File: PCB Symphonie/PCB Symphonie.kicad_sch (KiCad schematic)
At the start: 55 parts, among them J1 Neopixel Clavier, J2 Neopixel Indicateur batterie, SW0 SW_Push, SW1 SW_Push, SW10 SW_Push, SW11 SW_Push, SW12 SW_Push, SW13 SW_Push, SW14 SW_Push, SW15 SW_Push, SW16 SW_Push, SW17 SW_Push, SW18 SW_Push, SW19 SW_Push, SW2 SW_Push, SW20 SW_Push, SW21 SW_Push, SW22 SW_Push, SW23 SW_Push, SW24 SW_Push, SW3 SW_Push, SW4 SW_Push, SW5 SW_Push, SW6 SW_Push, SW7 SW_Push, SW8 SW_Push, SW9 SW_Push

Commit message: MAJ pcb
ajout alim remplacement esp32 par connecteur
Verifier taille condensateur (polarisation),
demander a augustin res de puissances,
replacer bouttons par piste et bornier
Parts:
- removed A1: Arduino_Nano_ESP32, Module:Arduino_Nano, symbol MCU_Module:Arduino_Nano_ESP32
- added BT1: Battery_Cell, symbol Device:Battery_Cell
- added C1, C10, C11, C12, C2, C3, C4, C5, C6, C7, C8, C9: C, symbol Device:C
- added D25, D27: LED, symbol Device:LED
- added D28: 1N4148, Diode_THT:D_DO-35_SOD27_P7.62mm_Horizontal, symbol Diode:1N4148
- added F1: Fuse, symbol Device:Fuse
- added J3: Bornier Alim Ampli, Connector:JWT_A3963_1x02_P3.96mm_Vertical, symbol Connector:Conn_01x02_Pin
- added J4: Bornier Signal ampli, Connector:JWT_A3963_1x02_P3.96mm_Vertical, symbol Connector:Conn_01x02_Pin
- added J5, J6: Conn_01x15_Pin, symbol Connector:Conn_01x15_Pin
- added P1: USB_C_Plug_USB2.0, symbol Connector:USB_C_Plug_USB2.0
- added Q1, Q2, Q3, Q4: 2N3905, Package_TO_SOT_THT:TO-3P-3_Horizontal_TabDown, symbol Transistor_BJT:2N3905
- added R1, R10, R11, R12, R13, R14, R15, R16, R17, R2, R3, R4, R5, R6, R7, R8, R9: R, Resistor_THT:R_Axial_DIN0204_L3.6mm_D1.6mm_P7.62mm_Horizontal, symbol Device:R
- added SW25: SW_Push_Open, symbol Switch:SW_Push_Open
- added U1, U2, U3, U4: LM317_TO-220, Package_TO_SOT_SMD:SOT-89-3_Handsoldering, symbol Regulator_Linear:LM317_TO-220
- renumbered D1 to D26
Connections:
- net GND is gone; now on net Earth: RV1.3
- net AMPLIFIER INPUT: now also J4.2 (Pin_2)
- net BATT LVL INPUT: now also R15.2, R16.1
- net COL0: now also J5.10 (Pin_10)
- net COL1: now also J5.9 (Pin_9)
- net COL2: now also J5.7 (Pin_7)
- net Earth: now also D26.1 (K), BT1.2 (-), C10.2, C11.2, C12.2, C4.2, C5.2, C6.2, C7.2, C8.2, C9.2, D27.1 (K), J3.1 (Pin_1), J4.1 (Pin_1), J5.14 (Pin_14), J6.2 (Pin_2), J6.3 (Pin_3), J6.5 (Pin_5), J6.8 (Pin_8), P1.A1 (GND), P1.A12 (GND), P1.B1 (GND), P1.B12 (GND), R11.1, R14.1, R16.2, R17.1, R8.1
- net GND MC: no longer D26.1 (K)
- net NEOPIX 1: now also J5.1 (Pin_1)
- net 5V renamed 5V Alim
- net 5V Alim: now also C8.1, C9.1, Q3.3 (C), R10.2, U3.2 (VO)
- new net: C1.2, C2.2, C3.2, D25.1 (K), R3.1
- new net: R2.1, R3.2, U1.1 (ADJ)
- new net: P1.A5 (CC), R17.2
- new net: BT1.1 (+), F1.2, SW25.1 (A)
- new net: Q2.1 (E), Q3.1 (E), Q4.1 (E), R12.2, R15.1, R5.2, R6.2, R9.2, SW25.2 (B)
- new net: C10.1, Q4.2 (B), R12.1, U4.3 (VI)
- new net: D25.2 (A), R4.1
- new net: C3.1, D28.2 (A), Q1.3 (C), R2.2, R4.2, U1.2 (VO)
- new net: C4.1, Q2.2 (B), R6.1, U2.3 (VI)
- new net: R10.1, R11.2, U3.1 (ADJ)
- new net: R7.1, R8.2, U2.1 (ADJ)
- new net: C7.1, Q3.2 (B), R9.1, U3.3 (VI)
- new net: D28.1 (K), F1.1
- new net: C1.1, P1.A4 (VBUS), P1.A9 (VBUS), P1.B4 (VBUS), P1.B9 (VBUS), Q1.1 (E), R1.1
- new net: C2.1, Q1.2 (B), R1.2, U1.3 (VI)
- new net: R13.1, R14.2, U4.1 (ADJ)
- new net: C11.1, C12.1, J3.2 (Pin_2), Q4.3 (C), R13.2, U4.2 (VO)
- new net: D27.2 (A), R5.1
- new net 3v3: C5.1, C6.1, J5.15 (Pin_15), Q2.3 (C), R7.2, U2.2 (VO)
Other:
- moved on the sheet: D26

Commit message: MAJ Pin changement shematique verifier empreintes
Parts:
- removed BT1: Battery_Cell, symbol Device:Battery_Cell
- removed C1, C12, C6, C9: C, symbol Device:C
- removed D15, D16, D17, D18, D19, D20, D21, D22, D23, D24: 1N4148, Diode_THT:D_DO-35_SOD27_P7.62mm_Horizontal, symbol Diode:1N4148
- removed J1: Neopixel Clavier, Connector_PinHeader_2.54mm:PinHeader_1x04_P2.54mm_Vertical, symbol Connector:Conn_01x04_Pin
- removed J2: Neopixel Indicateur batterie, Connector_PinHeader_2.54mm:PinHeader_1x04_P2.54mm_Vertical, symbol Connector:Conn_01x04_Pin
- removed SW0, SW1, SW10, SW11, SW12, SW13, SW14, SW15, SW16, SW17, SW18, SW19, SW2, SW20, SW21, SW22, SW23, SW24, SW3, SW4, SW5, SW6, SW7, SW8, SW9: SW_Push, Button_Switch_THT:SW_Tactile_Straight_KSA0Axx1LFTR, symbol Switch:SW_Push
- added C1, C12, C6, C9: C_Polarized_Small, Capacitor_SMD:CP_Elec_5x5.4, symbol Device:C_Polarized_Small
- added J1: Neopix batt, Connector:JWT_A3963_1x02_P3.96mm_Vertical, symbol Connector:Conn_01x02_Pin
- added J10, J9: Bornier alim neopix, Connector:JWT_A3963_1x02_P3.96mm_Vertical, symbol Connector:Conn_01x02_Pin
- added J2: Neopix piano, Connector:JWT_A3963_1x02_P3.96mm_Vertical, symbol Connector:Conn_01x02_Pin
- added J7: Conn_01x12_Pin, Connector_PinSocket_2.54mm:PinSocket_1x12_P2.54mm_Vertical, symbol Connector:Conn_01x12_Pin
- added R18, R19: R, Resistor_THT:R_Axial_DIN0204_L3.6mm_D1.6mm_P7.62mm_Horizontal, symbol Device:R
- C10, C11, C2, C3, C4, C5, C7, C8: footprint (none) -> Capacitor_THT:CP_Radial_D8.0mm_P3.80mm
- D25, D26, D27: footprint (none) -> LED_THT:LED_D3.0mm
- J5, J6: footprint (none) -> Connector_PinHeader_2.54mm:PinHeader_1x15_P2.54mm_Vertical
- Q1, Q2, Q3, Q4: footprint Package_TO_SOT_THT:TO-3P-3_Horizontal_TabDown -> Package_TO_SOT_THT:TO-3P-3_Vertical
- RV1: footprint Potentiometer_SMD:Potentiometer_ACP_CA6-VSMD_Vertical -> Potentiometer_THT:Potentiometer_ACP_CA9-H5_Horizontal
- SW25: footprint (none) -> Connector_USB:USB_C_Plug_JAE_DX07P024AJ1
- U1, U2, U3, U4: footprint Package_TO_SOT_SMD:SOT-89-3_Handsoldering -> Package_TO_SOT_THT:TO-3P-3_Vertical
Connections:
- net COL0 is gone; now on net Earth: J5.10 (Pin_10)
- net COL1 is gone; now on net Earth: J5.9 (Pin_9)
- net COL2 is gone; now on net Earth: J5.7 (Pin_7)
- net 3v3: now also C9.1
- net AMPLIFIER INPUT: now also J6.8 (Pin_8)
- net BATT LVL INPUT: now also J6.2 (Pin_2)
- net COL3: now also J6.12 (Pin_12), J7.4 (Pin_4), J7.8 (Pin_8)
- net COL4: now also J6.7 (Pin_7), J7.5 (Pin_5), J7.9 (Pin_9)
- net Earth: now also J6.14 (Pin_14), C1.2, C6.2, C9.2, J1.1 (Pin_1), J10.1 (Pin_1), J2.1 (Pin_1), J9.1 (Pin_1); no longer J6.2 (Pin_2), J6.3 (Pin_3), J6.5 (Pin_5), J6.8 (Pin_8)
- net LED BLE: now also J5.5 (Pin_5)
- net NEOPIX 1: now also R19.2
- net NEOPIX 2: now also J5.2 (Pin_2), R18.1
- net Volume INPUT: now also J6.1 (Pin_1)
- net at C2.2, C3.2, D25.1 (K)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: now also C12.2
- net at F1.2, SW25.1 (A): now also J10.2 (Pin_2)
- net at P1.A4 (VBUS), P1.A9 (VBUS), P1.B4 (VBUS)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: now also C12.1
- net at C11.1, J3.2 (Pin_2), Q4.3 (C)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: now also C1.1
- net ROW3: now reaches J5.12 (Pin_12)
- net ROW4: now reaches J5.6 (Pin_6)
- net A#: now reaches J6.10 (Pin_10)
- net A#: now also J6.11 (Pin_11), J7.11 (Pin_11), J7.12 (Pin_12), J7.2 (Pin_2), J7.3 (Pin_3), J7.7 (Pin_7)
- net A: now reaches J6.13 (Pin_13)
- net A: now also J7.1 (Pin_1), J7.10 (Pin_10), J7.6 (Pin_6)
- net 5V Alim: no longer names the net of C8.1, Q3.3 (C), R10.2, U3.2 (VO)
- net 5V Alim: now also C6.1, J9.2 (Pin_2)
- new net: J2.2 (Pin_2), R19.1
- new net: J1.2 (Pin_2), R18.2
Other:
- moved on the sheet: J3, J6, RV1

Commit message: Modif shema, Alim fait par simon
Debut PCB
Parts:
- removed C1, C12, C6, C9: C_Polarized_Small, Capacitor_SMD:CP_Elec_5x5.4, symbol Device:C_Polarized_Small
- removed C10, C11, C2, C3, C4, C5, C7, C8: C, Capacitor_THT:CP_Radial_D8.0mm_P3.80mm, symbol Device:C
- removed D25, D27: LED, LED_THT:LED_D3.0mm, symbol Device:LED
- removed D28: 1N4148, Diode_THT:D_DO-35_SOD27_P7.62mm_Horizontal, symbol Diode:1N4148
- removed F1: Fuse, symbol Device:Fuse
- removed J10, J9: Bornier alim neopix, Connector:JWT_A3963_1x02_P3.96mm_Vertical, symbol Connector:Conn_01x02_Pin
- removed P1: USB_C_Plug_USB2.0, symbol Connector:USB_C_Plug_USB2.0
- removed Q1, Q2, Q3, Q4: 2N3905, Package_TO_SOT_THT:TO-3P-3_Vertical, symbol Transistor_BJT:2N3905
- removed R1, R10, R11, R12, R13, R14, R15, R16, R17, R2, R3, R4, R5, R6, R7, R8, R9: R, Resistor_THT:R_Axial_DIN0204_L3.6mm_D1.6mm_P7.62mm_Horizontal, symbol Device:R
- removed SW25: SW_Push_Open, Connector_USB:USB_C_Plug_JAE_DX07P024AJ1, symbol Switch:SW_Push_Open
- removed U1, U2, U3, U4: LM317_TO-220, Package_TO_SOT_THT:TO-3P-3_Vertical, symbol Regulator_Linear:LM317_TO-220
- added J11: Conn_01x12_Pin, Connector_PinSocket_2.54mm:PinSocket_1x12_P2.54mm_Vertical, symbol Connector:Conn_01x12_Pin
- added J12, J13, J8: Neopix batt, Connector:JWT_A3963_1x02_P3.96mm_Vertical, symbol Connector:Conn_01x02_Pin
- J3: value Bornier Alim Ampli -> Alim ESP32
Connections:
- net 3v3: now also J3.2 (Pin_2)
- net R_BT2: now reaches D13.2 (A)
- net R_BT2: now also J12.2 (Pin_2)
- net R_BT1: now reaches D12.2 (A)
- net R_BT1: now also J8.2 (Pin_2)
- net RC: now reaches D0.2 (A)
- net RC: now also J11.1 (Pin_1)
- net RE: now reaches D4.2 (A)
- net RE: now also J11.5 (Pin_5)
- net RG#: now reaches D8.2 (A)
- net RG#: now also J11.9 (Pin_9)
- net RF#: now reaches D6.2 (A)
- net RF#: now also J11.7 (Pin_7)
- net RD: now reaches D2.2 (A)
- net RD: now also J11.3 (Pin_3)
- net RG: now reaches D7.2 (A)
- net RG: now also J11.8 (Pin_8)
- net RA: now reaches D9.2 (A)
- net RA: now also J11.10 (Pin_10)
- net RF: now reaches D5.2 (A)
- net RF: now also J11.6 (Pin_6)
- net RB: now reaches D11.2 (A)
- net RB: now also J11.12 (Pin_12)
- net RC#: now reaches D1.2 (A)
- net RC#: now also J11.2 (Pin_2)
- net RA#: now reaches D10.2 (A)
- net RA#: now also J11.11 (Pin_11)
- net RD#: now reaches D3.2 (A)
- net RD#: now also J11.4 (Pin_4)
- net R_BT3: now reaches D14.2 (A)
- net R_BT3: now also J13.2 (Pin_2)
- net A renamed CA#
- net CA#: now also J7.11 (Pin_11); no longer J7.10 (Pin_10)
- net A# renamed CB
- net CB: no longer J6.11 (Pin_11), J7.11 (Pin_11), J7.3 (Pin_3)
- net COL3 renamed CD#
- net CD#: now also J7.9 (Pin_9), J12.1 (Pin_1); no longer J7.8 (Pin_8)
- net COL4 renamed CA
- net CA: now also J7.10 (Pin_10), J13.1 (Pin_1); no longer J7.9 (Pin_9)
- new net CD: J6.11 (Pin_11), J7.3 (Pin_3), J7.8 (Pin_8), J8.1 (Pin_1)
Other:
- moved on the sheet: D0, D1, D2, D3, D4, RV1

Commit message: maj pcb
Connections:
- net ROW3: no longer names the net of J5.12 (Pin_12)
- net ROW4: no longer names the net of J5.6 (Pin_6)

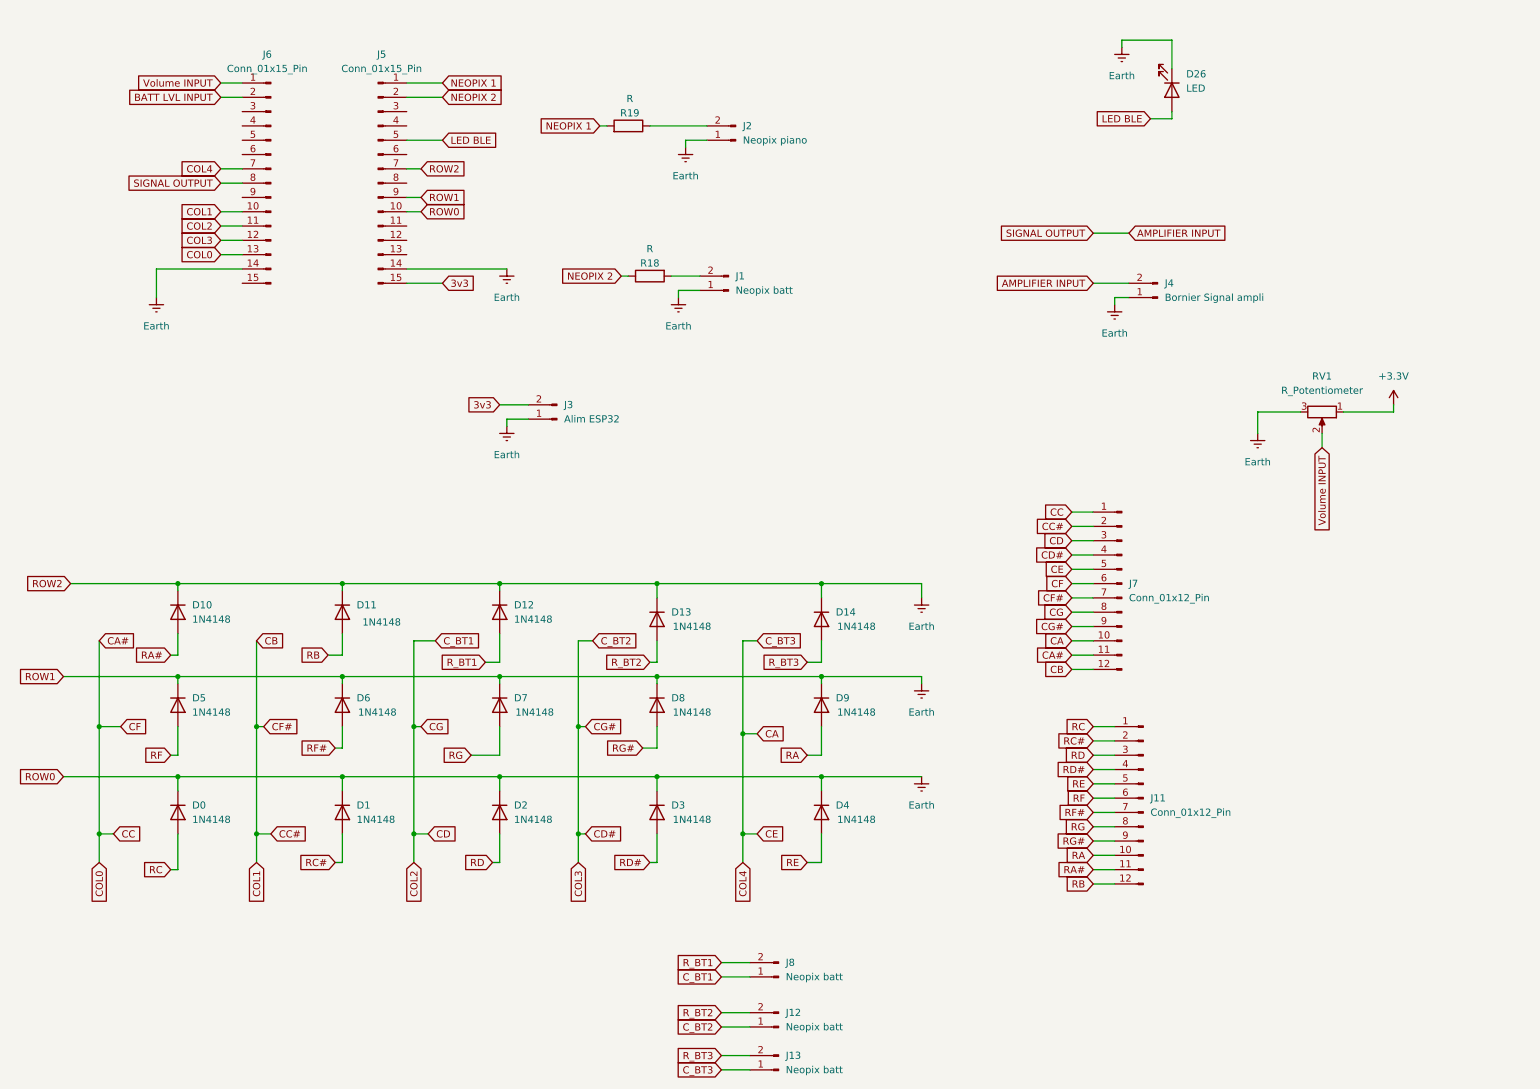
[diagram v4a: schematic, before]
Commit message: Routage bien avancer ajout mode auto
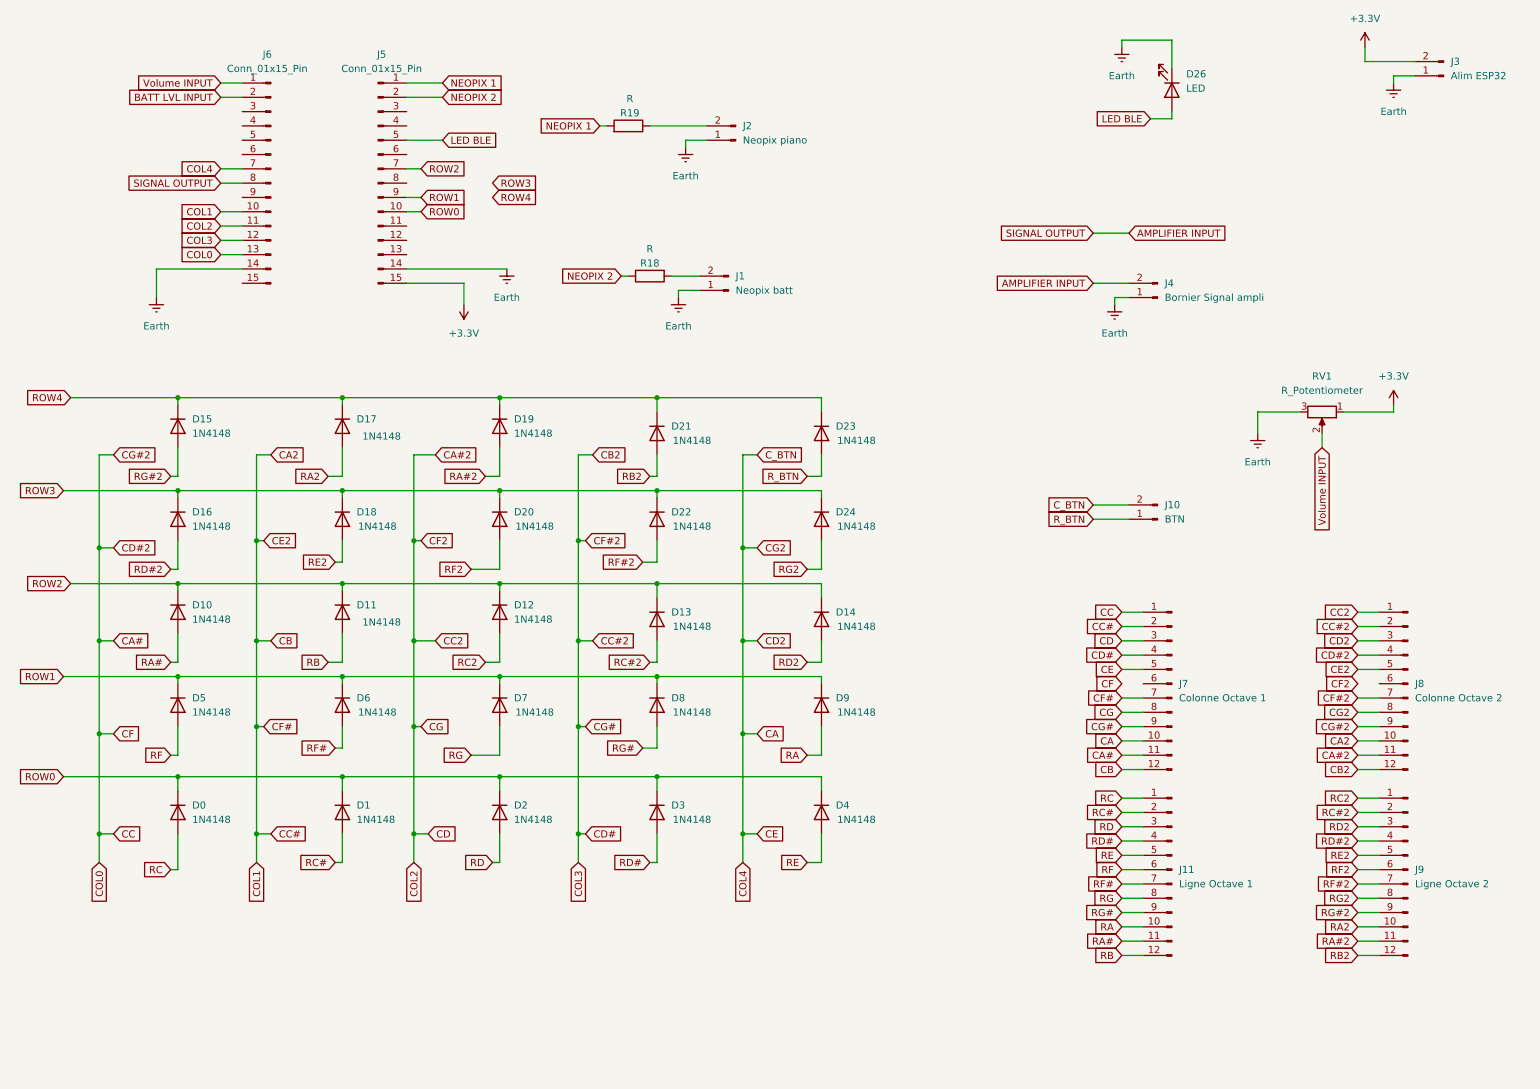
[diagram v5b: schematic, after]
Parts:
- removed J12, J13, J8: Neopix batt, Connector:JWT_A3963_1x02_P3.96mm_Vertical, symbol Connector:Conn_01x02_Pin
- added D15, D16, D17, D18, D19, D20, D21, D22, D23, D24: 1N4148, Diode_THT:D_DO-35_SOD27_P7.62mm_Horizontal, symbol Diode:1N4148
- added J10: BTN, Connector:JWT_A3963_1x02_P3.96mm_Vertical, symbol Connector:Conn_01x02_Pin
- added J8: Colonne Octave 2, Connector_PinSocket_2.54mm:PinSocket_1x12_P2.54mm_Vertical, symbol Connector:Conn_01x12_Pin
- added J9: Ligne Octave 2, Connector_PinSocket_2.54mm:PinSocket_1x12_P2.54mm_Vertical, symbol Connector:Conn_01x12_Pin
- J11: value Conn_01x12_Pin -> Ligne Octave 1
- J7: value Conn_01x12_Pin -> Colonne Octave 1
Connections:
- net 3v3 is gone; now on net +3.3V: J3.2 (Pin_2), J5.15 (Pin_15)
- net CA: now also J10.2 (Pin_2), J8.3 (Pin_3), J8.8 (Pin_8)
- net CA#: now also J8.4 (Pin_4), J8.9 (Pin_9); no longer J7.6 (Pin_6)
- net Earth: no longer D0.1 (K), D1.1 (K), D10.1 (K), D11.1 (K), D12.1 (K), D13.1 (K), D14.1 (K), D2.1 (K), D3.1 (K), D4.1 (K), D5.1 (K), D6.1 (K), D7.1 (K), D8.1 (K), D9.1 (K), J5.10 (Pin_10), J5.7 (Pin_7), J5.9 (Pin_9)
- net CB renamed CA2
- net CA2: now also J8.10 (Pin_10), J8.5 (Pin_5)
- net CD renamed CA#2
- net CA#2: now also J8.1 (Pin_1), J8.11 (Pin_11)
- net CD# renamed CB2
- net CB2: now also J8.12 (Pin_12), J8.2 (Pin_2), J8.7 (Pin_7)
- net R_BT1 renamed RC2
- net RC2: now also J9.1 (Pin_1)
- net R_BT2 renamed RC#2
- net RC#2: now also J9.2 (Pin_2)
- net R_BT3 renamed RD2
- net RD2: now also J9.3 (Pin_3)
- new net RA#2: D19.2 (A), J9.11 (Pin_11)
- new net RA2: D17.2 (A), J9.10 (Pin_10)
- new net RB2: D21.2 (A), J9.12 (Pin_12)
- new net RD#2: D16.2 (A), J9.4 (Pin_4)
- new net RE2: D18.2 (A), J9.5 (Pin_5)
- new net RF#2: D22.2 (A), J9.7 (Pin_7)
- new net RF2: D20.2 (A), J9.6 (Pin_6)
- new net RG#2: D15.2 (A), J9.9 (Pin_9)
- new net RG2: D24.2 (A), J9.8 (Pin_8)
- new net ROW0: D0.1 (K), D1.1 (K), D2.1 (K), D3.1 (K), D4.1 (K), J5.10 (Pin_10)
- new net ROW1: D5.1 (K), D6.1 (K), D7.1 (K), D8.1 (K), D9.1 (K), J5.9 (Pin_9)
- new net ROW2: D10.1 (K), D11.1 (K), D12.1 (K), D13.1 (K), D14.1 (K), J5.7 (Pin_7)
- new net ROW3: D16.1 (K), D18.1 (K), D20.1 (K), D22.1 (K), D24.1 (K)
- new net ROW4: D15.1 (K), D17.1 (K), D19.1 (K), D21.1 (K), D23.1 (K)
- new net R_BTN: D23.2 (A), J10.1 (Pin_1)
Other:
- moved on the sheet: J11, J3, J7

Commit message: Fin cours 4mars
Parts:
- removed J1: Neopix batt, Connector:JWT_A3963_1x02_P3.96mm_Vertical, symbol Connector:Conn_01x02_Pin
- removed J10: BTN, Connector:JWT_A3963_1x02_P3.96mm_Vertical, symbol Connector:Conn_01x02_Pin
- removed J2: Neopix piano, Connector:JWT_A3963_1x02_P3.96mm_Vertical, symbol Connector:Conn_01x02_Pin
- removed J3: Alim ESP32, Connector:JWT_A3963_1x02_P3.96mm_Vertical, symbol Connector:Conn_01x02_Pin
- removed J4: Bornier Signal ampli, Connector:JWT_A3963_1x02_P3.96mm_Vertical, symbol Connector:Conn_01x02_Pin
- removed RV1: R_Potentiometer, Potentiometer_THT:Potentiometer_ACP_CA9-H5_Horizontal, symbol Device:R_Potentiometer
- added D25: LED, LED_THT:LED_D3.0mm, symbol Device:LED
- added J1: Neopix Batt, TerminalBlock:TerminalBlock_MaiXu_MX126-5.0-02P_1x02_P5.00mm, symbol Connector:Screw_Terminal_01x02
- added J10: BTN, TerminalBlock:TerminalBlock_MaiXu_MX126-5.0-02P_1x02_P5.00mm, symbol Connector:Screw_Terminal_01x02
- added J2: Neopix piano, TerminalBlock:TerminalBlock_MaiXu_MX126-5.0-02P_1x02_P5.00mm, symbol Connector:Screw_Terminal_01x02
- added J3: Alim ESP32, TerminalBlock:TerminalBlock_MaiXu_MX126-5.0-02P_1x02_P5.00mm, symbol Connector:Screw_Terminal_01x02
- added J4: Bornier Signal Ampli, TerminalBlock:TerminalBlock_MaiXu_MX126-5.0-02P_1x02_P5.00mm, symbol Connector:Screw_Terminal_01x02
- added R1: R, Resistor_THT:R_Axial_DIN0204_L3.6mm_D1.6mm_P7.62mm_Horizontal, symbol Device:R
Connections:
- net +3.3V: now also J3.1 (Pin_1), R1.2
- net AMPLIFIER INPUT: now also J4.1 (Pin_1)
- net CA: now also J7.6 (Pin_6), J7.7 (Pin_7), J8.6 (Pin_6), J8.7 (Pin_7), J10.1 (Pin_1); no longer J7.10 (Pin_10), J7.5 (Pin_5), J8.3 (Pin_3), J8.8 (Pin_8)
- net CA#: now also J7.10 (Pin_10), J7.8 (Pin_8), J7.9 (Pin_9), J8.5 (Pin_5); no longer J7.1 (Pin_1), J7.11 (Pin_11), J8.9 (Pin_9)
- net CA#2: now also J7.11 (Pin_11), J7.12 (Pin_12), J8.2 (Pin_2), J8.3 (Pin_3); no longer J7.3 (Pin_3), J7.8 (Pin_8), J8.11 (Pin_11)
- net CA2: now also J7.3 (Pin_3), J7.4 (Pin_4), J7.5 (Pin_5), J8.8 (Pin_8), J8.9 (Pin_9); no longer J7.12 (Pin_12), J7.2 (Pin_2), J7.7 (Pin_7), J8.10 (Pin_10), J8.5 (Pin_5)
- net CB2: now also J7.1 (Pin_1), J7.2 (Pin_2), J8.10 (Pin_10), J8.11 (Pin_11); no longer J7.4 (Pin_4), J7.9 (Pin_9), J8.2 (Pin_2), J8.7 (Pin_7)
- net Earth: now also D25.2 (A), J1.2 (Pin_2), J2.2 (Pin_2), J3.2 (Pin_2), J4.2 (Pin_2)
- net ROW3: now also J5.11 (Pin_11)
- net ROW4: now also J5.6 (Pin_6)
- net R_BTN: now also J10.2 (Pin_2)
- net at R19.1: now also J2.1 (Pin_1)
- net at R18.2: now also J1.1 (Pin_1)
- new net: D25.1 (K), R1.1
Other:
- moved on the sheet: R18, R19
